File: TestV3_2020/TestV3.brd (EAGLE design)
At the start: 100 x 100 mm, 112 parts, among them J4 XT30UPB-F, J5 CONN_03, J6 XT30UPB-F, Q3 600mA/40V, Q4 600mA/40V, U2 MP2451

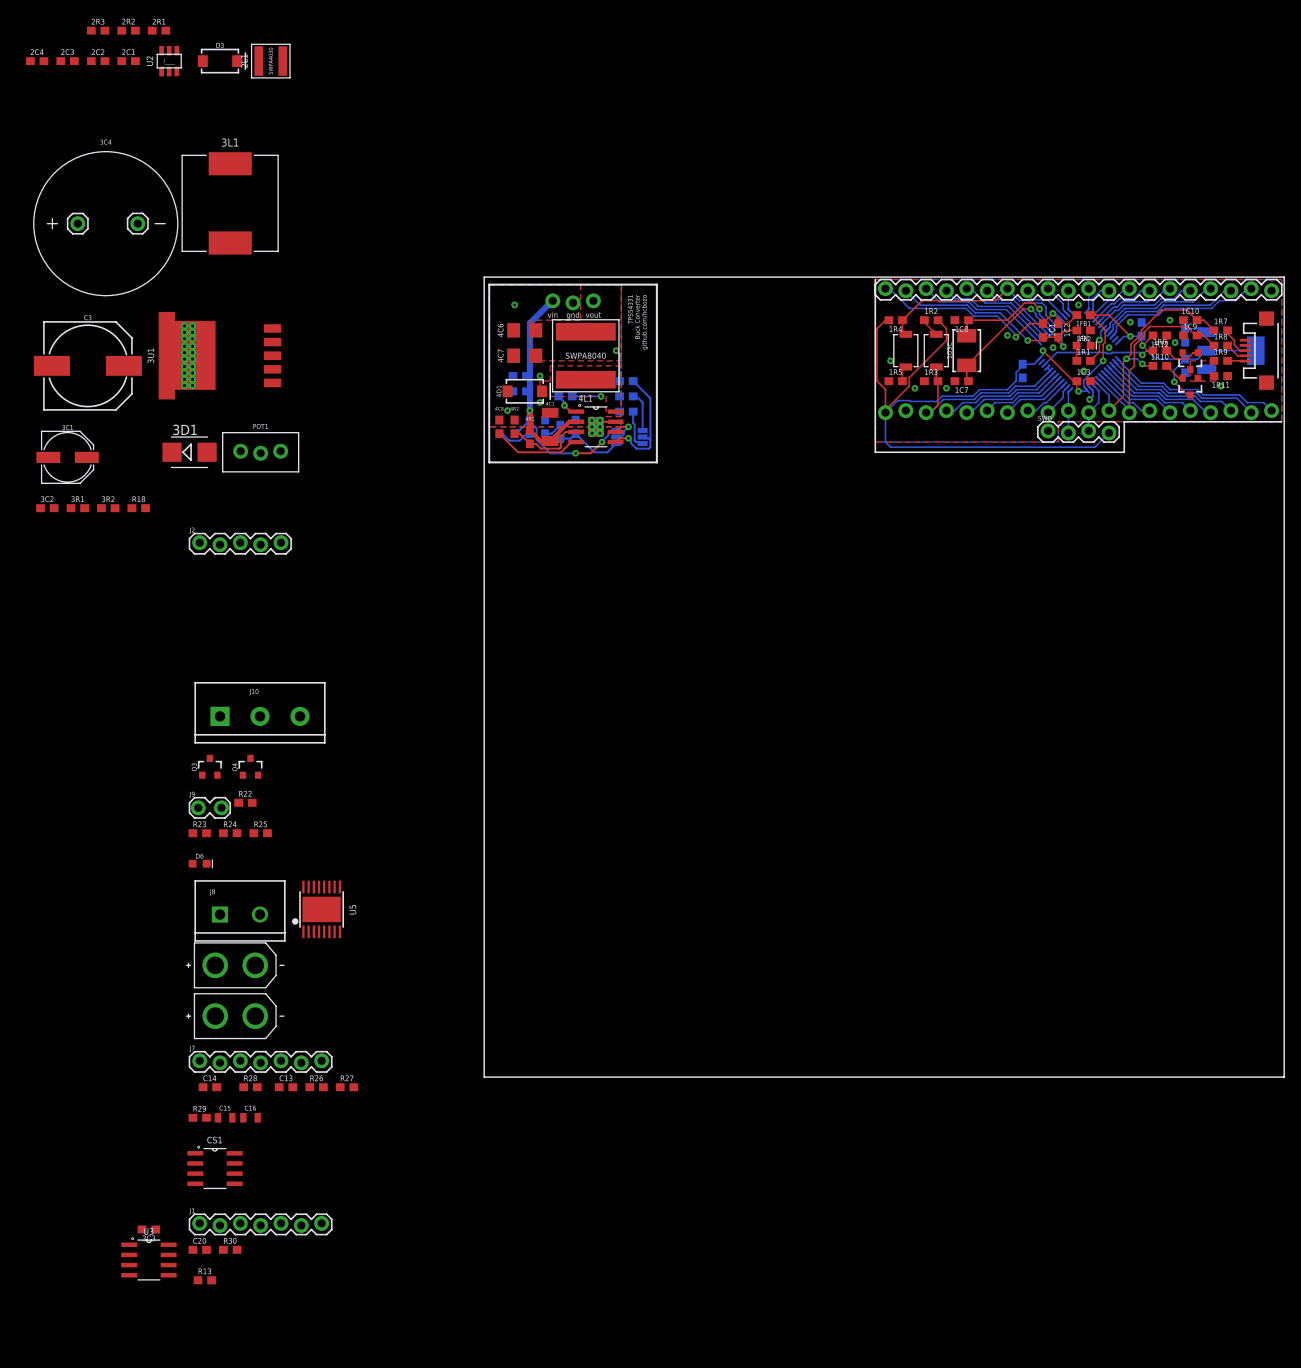
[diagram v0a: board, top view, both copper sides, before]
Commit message: MP2451 Buck Converter Circuit
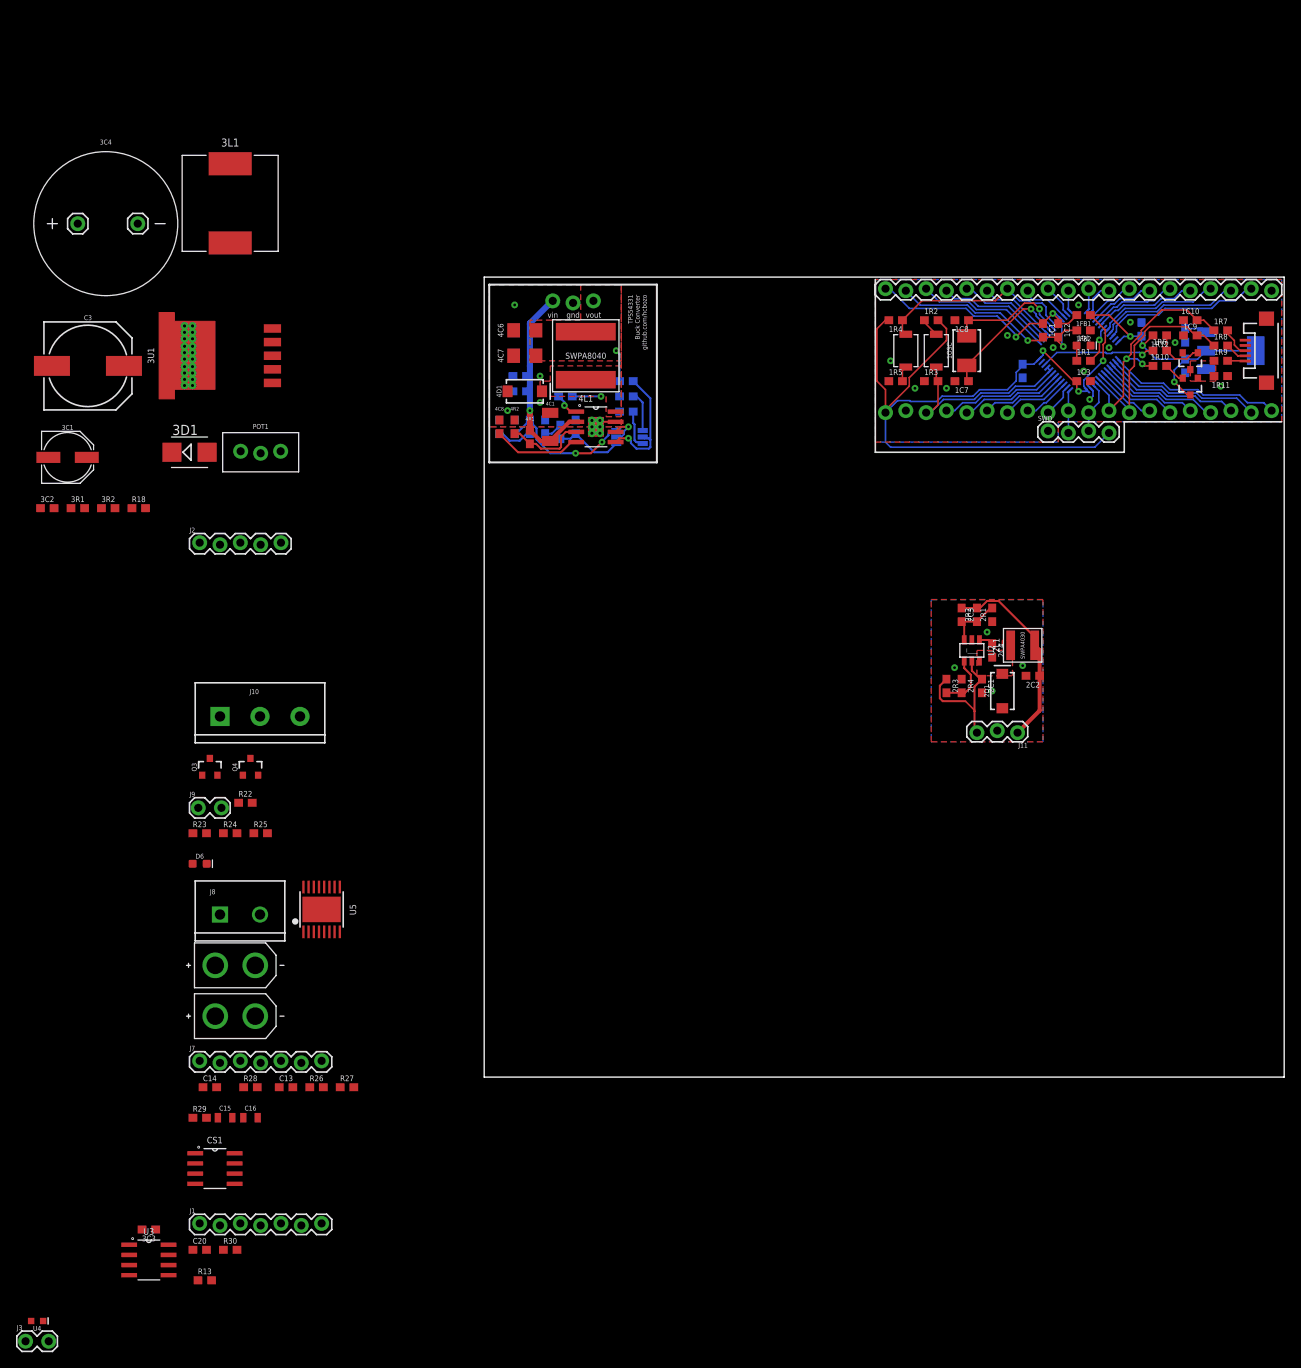
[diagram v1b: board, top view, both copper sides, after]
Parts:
- removed D3: SS34, JH:SMA-DIODE
- added 2D1: SS34, JH:SMA-DIODE
- added 2R4: 20k, JH:R0603
- added J11: CONN_03, JH:1X03_LOCK
- added J3: (no value), SparkFun-Connectors:1X02_LOCK
- added U4: LIGHT_SENSORALS, SparkFun-Sensors:ALS-PT19
- 2L1: value 4.7uH -> 3.3uH
- 2R1: value 124k -> 40.2k
- 2R2: value 40.2k -> 124k
- 2R3: value >33k -> 39k
- moved 2C4 140.3 mm to (63.5, 53.3), turned to 270 degrees
- moved 2C2 139.8 mm to (68.6, 50.2), turned to 180 degrees
- moved 2R3 134.0 mm to (57.8, 48.9), turned to 270 degrees
- moved 2C1 132.2 mm to (62.2, 48.9), turned to 270 degrees
- moved 2C3 131.5 mm to (59.7, 57.8), turned to 270 degrees
- moved 2R2 128.8 mm to (61.6, 57.8), turned to 90 degrees
- moved 2R1 127.2 mm to (63.5, 57.8), turned to 90 degrees
- moved U2 124.5 mm to (61.0, 53.3), turned to 180 degrees
- moved 2L1 119.0 mm to (67.3, 54.0)
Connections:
- removed net N$7: 2R3.2, U2.P4
- new net N$14: J3.2, U4.C
- new net N$17: J3.1, U4.E
- new net N$20: 2R3.2, 2R4.2, U2.P4
- net GND-BUCK: now also 2D1.A, 2R1.1, 2R4.1, J11.2; no longer 2R2.1, D3.A
- net N$3: now also 2R1.2, 2R2.1; no longer 2R1.1, 2R2.2
- net N$5: now also 2D1.C; no longer D3.C
- net VIN-BUCK: now also 2R3.1, J11.3
- net VOUT-BUCK: now also 2R2.2, J11.1; no longer 2R1.2, 2R3.1
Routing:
- net VOUT-BUCK: track 0.00 -> 24.7 mm
- net VIN-BUCK: track 0.00 -> 18.0 mm
- net N$20: track 0.00 -> 6.96 mm
- net N$3: track 0.00 -> 6.94 mm
- net N$6: track 0.00 -> 1.78 mm
- added copper zone on layer 1, net GND-BUCK
- added copper zone on layer 16, net GND-BUCK
- added copper zone on layer 1, net N$5

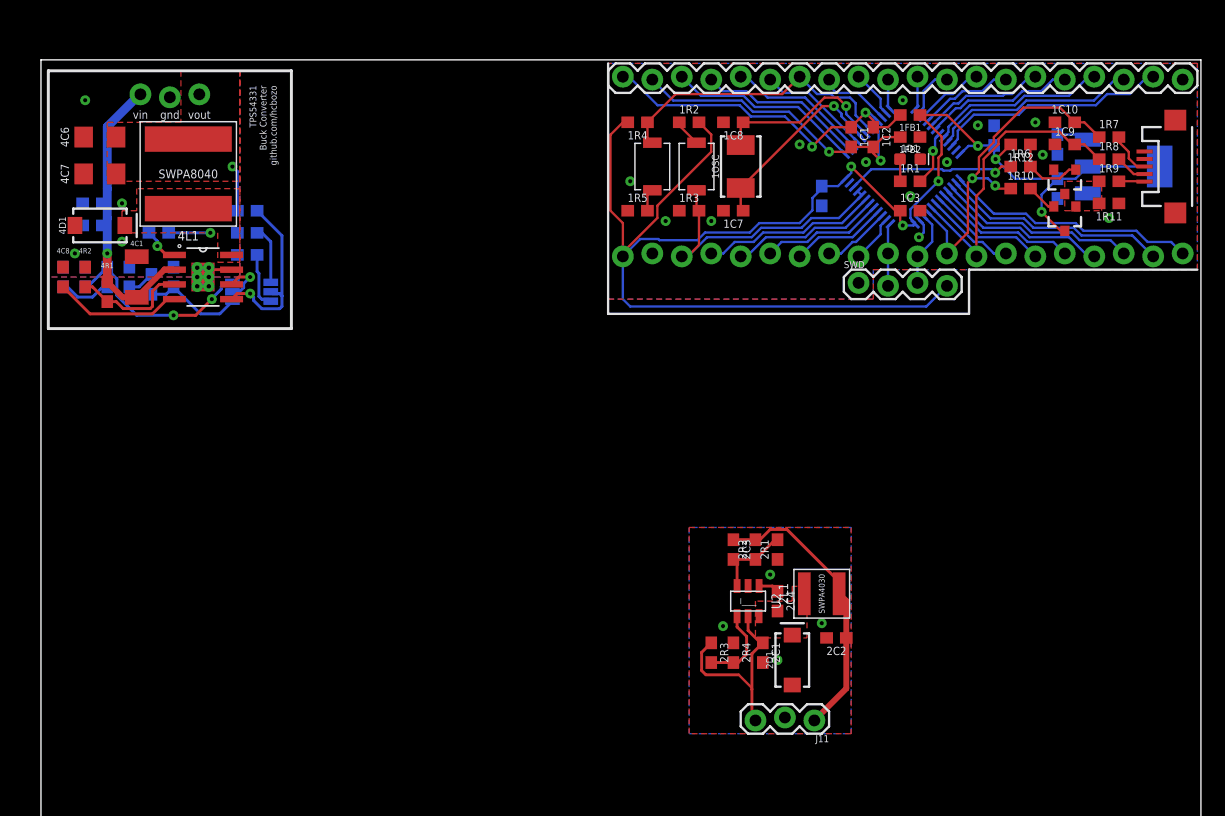
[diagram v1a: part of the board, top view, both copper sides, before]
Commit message: Fixed silkscreen for stm32 and mp2541
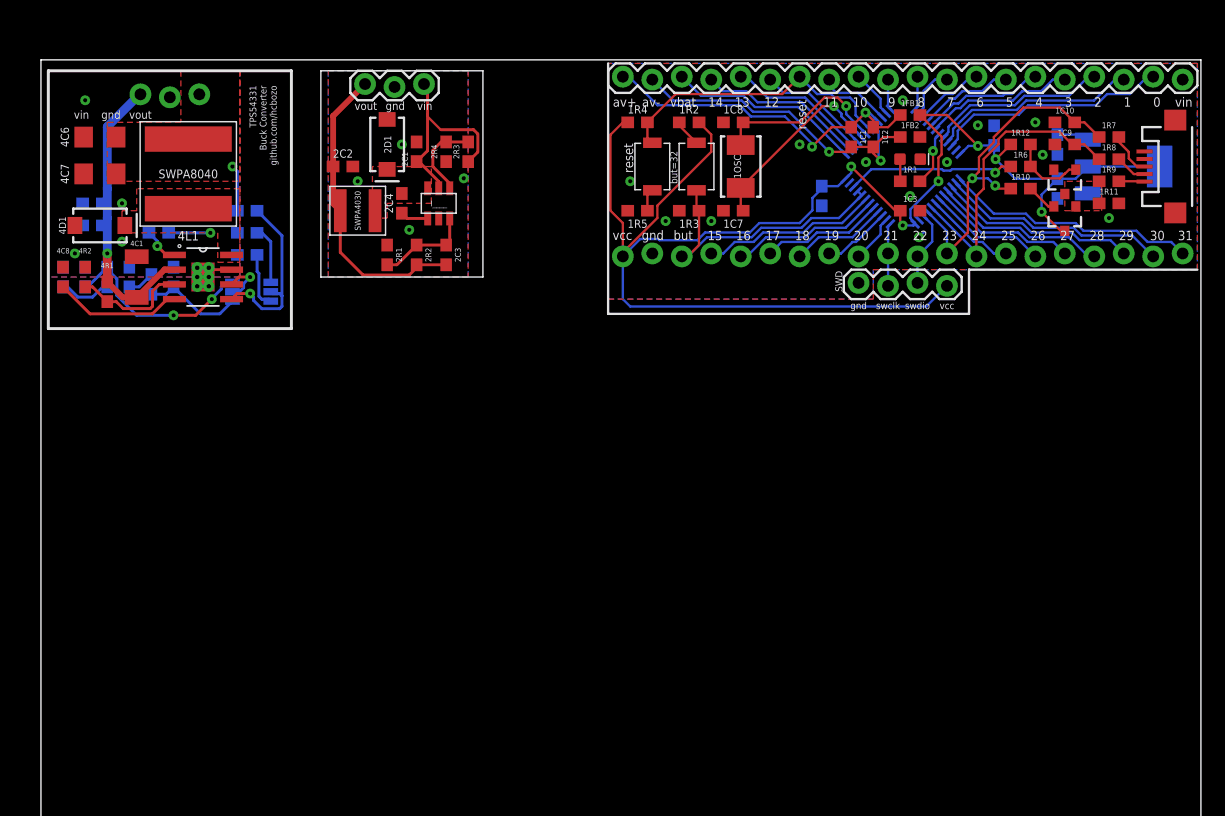
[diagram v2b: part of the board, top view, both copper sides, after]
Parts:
- moved J11 67.0 mm to (27.9, 97.8), turned to 0 degrees
- moved 2C2 58.8 mm to (26.0, 90.8), turned to 0 degrees
- moved 2D1 56.5 mm to (29.8, 92.7), turned to 270 degrees
- moved 2C1 52.5 mm to (32.4, 92.1), turned to 90 degrees
- moved 2L1 51.9 mm to (27.3, 87.0), turned to 180 degrees
- moved 2R4 49.8 mm to (34.9, 92.1), turned to 90 degrees
- moved 2R3 48.0 mm to (36.8, 92.1), turned to 90 degrees
- moved 2C4 47.2 mm to (31.1, 87.6), turned to 90 degrees
- moved U2 43.4 mm to (34.3, 87.6), turned to 0 degrees
- moved 2R1 42.2 mm to (29.8, 83.2), turned to 270 degrees
- moved 2R2 38.7 mm to (32.4, 83.2), turned to 270 degrees
- moved 2C3 35.5 mm to (34.9, 83.2), turned to 90 degrees
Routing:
- net VOUT-BUCK: track 24.7 -> 26.3 mm
- net N$3: track 6.94 -> 8.21 mm
- net GND: track 1.83 -> 0.58 mm
- net N$6: track 1.78 -> 2.41 mm
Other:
- board text added: "0"
- board text added: "1"
- board text added: "10"
- board text added: "11"
- board text added: "12"
- board text added: "13"
- board text added: "14"
- board text added: "15"
- board text added: "16"
- board text added: "17"
- board text added: "18"
- board text added: "19"
- board text added: "2"
- board text added: "20"
- board text added: "21"
- board text added: "22"
- board text added: "23"
- board text added: "24"
- board text added: "25"
- board text added: "26"
- board text added: "27"
- board text added: "28"
- board text added: "29"
- board text added: "3"
- board text added: "30"
- board text added: "31"
- board text added: "4"
- board text added: "5"
- board text added: "6"
- board text added: "7"
- board text added: "8"
- board text added: "9"
- board text added: "av+"
- board text added: "av-"
- board text added: "but"
- board text added: "but=32"
- board text added: "reset"
- board text added: "swclk"
- board text added: "swdio"
- board text added: "vbat"
- board text added: "vcc"

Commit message: finished all the board layouts
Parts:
- removed 3C4: 1000uF, JH:1000UF-CAP
- removed C3: 100uF, SparkFun-Capacitors:NIC_10X10.5_CAP
- removed POT1: 10k, JH:3296-TRIMPOT
- removed R13: 20k, JH:R0603
- removed R18: 45k, JH:R0603
- added 3C5: 0.1uF, JH:C0603
- added 3POT1: 10k, JH:3296-TRIMPOT
- added 3R3: 20k, JH:R0603
- added 3R4: 45k, JH:R0603
- added JP1: JUMPER-SMT_2_NO_NO-SILK_ROUND, SparkFun-Jumpers:SMT-JUMPER_2_NO_NO-SILK_ROUND
- 3C3: value 0.1uF -> 100uF; device JH:C0603 -> SparkFun-Capacitors:NIC_10X10.5_CAP
- moved U3 136.9 mm to (84.5, 29.8), turned to 90 degrees
- moved J9 136.5 mm to (96.5, 67.9), turned to 270 degrees
- moved 3C2 135.2 mm to (78.1, 45.1), turned to 90 degrees
- moved J2 135.1 mm to (92.7, 24.1), turned to 180 degrees
- moved R23 133.4 mm to (93.3, 64.8), turned to 270 degrees
- moved 3R1 132.3 mm to (78.1, 41.3), turned to 270 degrees
- moved 3R2 131.3 mm to (81.9, 46.4), turned to 90 degrees
- moved 3C1 129.1 mm to (72.4, 43.2), turned to 180 degrees
- moved 3U1 128.5 mm to (74.3, 26.7), turned to 90 degrees
- moved D6 128.3 mm to (87.0, 64.8), turned to 270 degrees
- moved Q3 128.3 mm to (90.2, 69.8), turned to 180 degrees
- moved R22 127.9 mm to (93.3, 68.6), turned to 270 degrees
- moved R24 127.2 mm to (90.2, 66.7)
- moved Q4 121.9 mm to (90.2, 63.5), turned to 180 degrees
- moved 3C3 121.5 mm to (74.3, 16.5)
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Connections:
- net FDBK: now also 3POT1.1, 3POT1.2, 3R3.1; no longer POT1.1, POT1.2, R13.1
- net GND-BOOST: now also 3C3.-, JP1.1; no longer 3C4.-, C3.-
- net GND-CS: now also J1.2; no longer J1.1
- net GND-POT: now also 3C5.2, J2.2, JP1.2; no longer 3C3.2, J2.1
- net N$16: now also 3POT1.3; no longer POT1.3
- net N$18: now also 3R3.2, 3R4.1; no longer R13.2, R18.1
- net VIN-CS: now also J1.1; no longer J1.2
- net VIN-POT: now also 3C5.1, J2.1; no longer 3C3.1, J2.2
- net VOUT-BOOST: now also 3C3.+, 3R4.2; no longer 3C4.+, C3.+, R18.2
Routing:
- net VIN-BOOST: track 0.00 -> 73.9 mm
- net VOUT-BOOST: track 0.00 -> 21.1 mm
- net FDBK: track 0.00 -> 20.2 mm
- net VCC-MOTOR: track 0.00 -> 20.0 mm, vias 0 -> 1
- net N$32: track 0.00 -> 19.2 mm, vias 0 -> 1
- net GND-POT: track 0.00 -> 16.7 mm
- net GND-LED: track 0.00 -> 16.4 mm
- net N$29: track 0.00 -> 15.9 mm, vias 0 -> 1
- net N$27: track 0.00 -> 15.8 mm, vias 0 -> 1
- net VIN-POT: track 0.00 -> 14.8 mm
- net VIN-LED: track 0.00 -> 14.4 mm, vias 0 -> 2
- net N$39: track 0.00 -> 14.3 mm
- net N$45: track 0.00 -> 13.8 mm
- net VIN-MOTOR: track 0.00 -> 13.5 mm
- net N$40: track 0.00 -> 12.8 mm
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- added copper zone on layer 1, net GND-BOOST
- added copper zone on layer 16, net GND-BOOST
- added copper zone on layer 1, net GND-MOTOR
- added copper zone on layer 16, net GND-MOTOR
- added copper zone on layer 1, net N$34
- added copper zone on layer 1, net VIN-BOOST
- added copper zone on layer 1, net VOUT-BOOST
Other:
- board text added: "cs"
- board text added: "light sensor test"
- board text added: "mosi"
- board text added: "sclk"
